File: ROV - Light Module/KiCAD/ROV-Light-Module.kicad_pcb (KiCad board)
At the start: 2 copper layers, 73.7 x 23.4 mm, 55 parts, among them J4 Bottom - Middle, J6 Main In, J7 Bottom - Middle, J8 Middle - Top, J9 Middle - Top, U1 AL8805W5, U2 ATtiny1614-Arduino, U3 AP63205WU, U6 MAX3072E

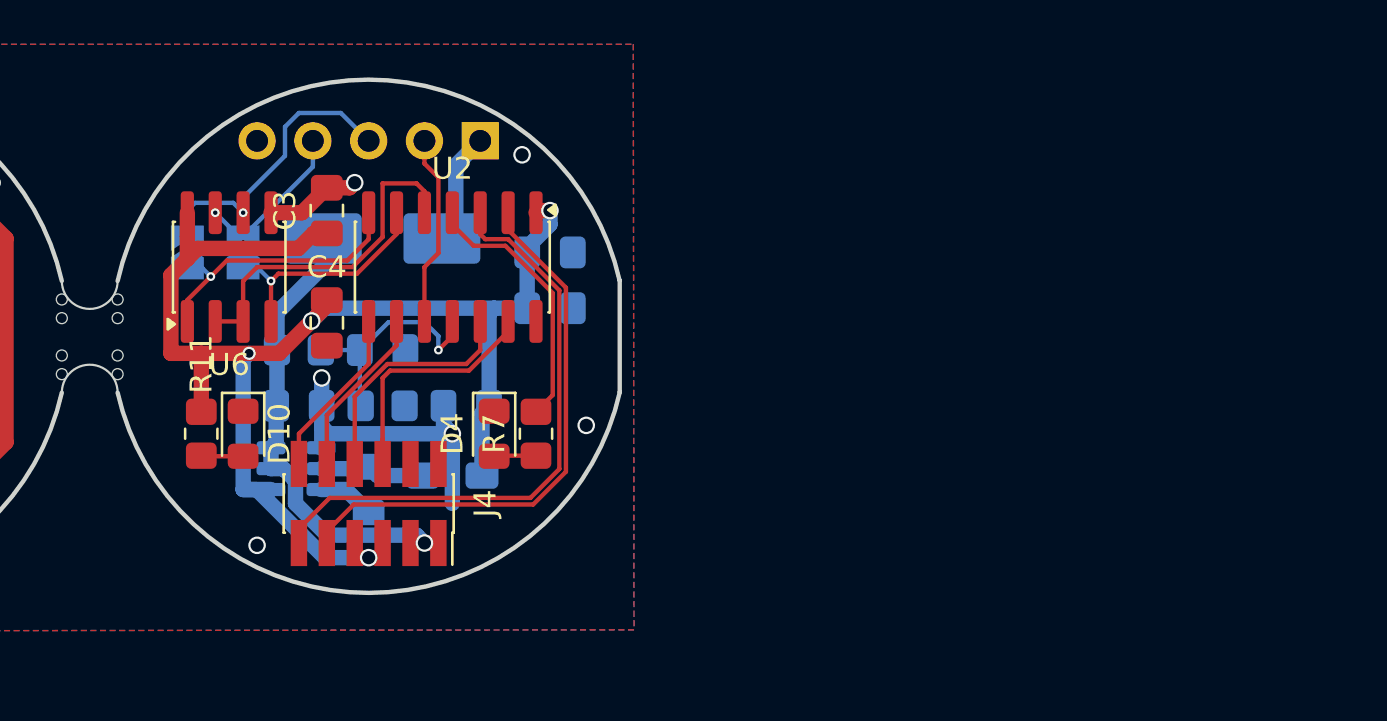
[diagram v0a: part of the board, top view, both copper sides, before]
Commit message: moved the arduino to seperet schematic
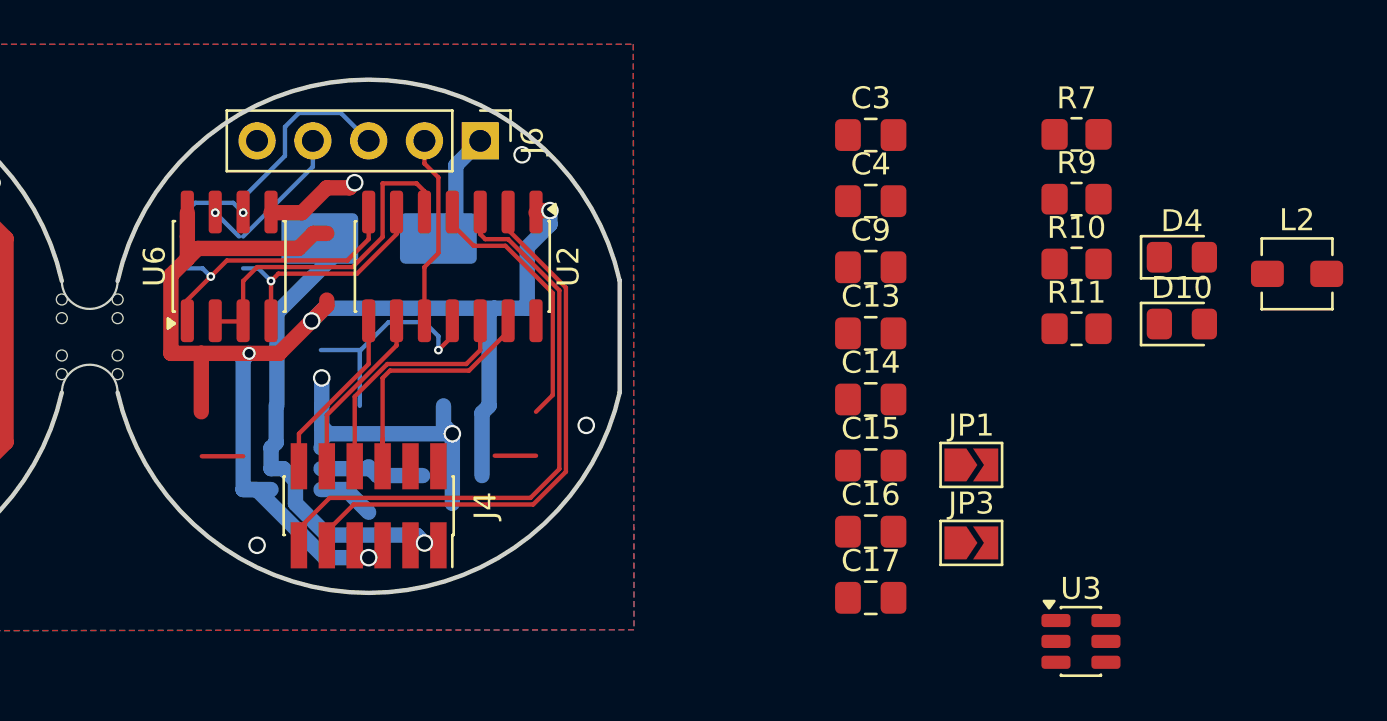
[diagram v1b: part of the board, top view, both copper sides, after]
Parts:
- removed JP2: RX, Jumper:SolderJumper-2_P1.3mm_Open_TrianglePad1.0x1.5mm
- added JP3: RX, Jumper:SolderJumper-2_P1.3mm_Open_TrianglePad1.0x1.5mm, F.Cu at (217.9, 85.6)
- C13, C14, C15, C16, C17, C9, J6, JP1, L2, R10, R9, U3: moved to F.Cu
- moved D10 43.0 mm to (227.5, 75.7), turned to 0 degrees
- moved R11 40.1 mm to (222.7, 75.9), turned to 0 degrees
- moved L2 39.5 mm to (232.8, 73.4)
- moved JP1 37.0 mm to (217.9, 82.1), turned to 0 degrees
- moved U3 36.6 mm to (222.9, 90.1)
- moved R9 36.1 mm to (222.7, 70.0)
- moved D4 32.3 mm to (227.5, 72.6), turned to 0 degrees
- moved R10 32.2 mm to (222.7, 72.9)
- moved R7 28.1 mm to (222.7, 67.0), turned to 0 degrees
- moved C14 26.0 mm to (213.4, 79.1), turned to 0 degrees
- moved C4 25.4 mm to (213.4, 70.1), turned to 0 degrees
- moved C3 25.0 mm to (213.4, 67.0), turned to 0 degrees
- moved C15 22.9 mm to (213.4, 82.1), turned to 0 degrees
- moved C13 22.2 mm to (213.4, 76.1)
- moved C17 21.5 mm to (213.4, 88.1), turned to 0 degrees
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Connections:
- net /A9/D9 renamed /Arduino Driver PCB/A9/D9
- net /Builtin_LED renamed /Arduino Driver PCB/Builtin_LED
- net /Data_A renamed /Arduino Driver PCB/Data_A
- net /Data_B renamed /Arduino Driver PCB/Data_B
- net /LED_PWM renamed /Arduino Driver PCB/LED_PWM
- net /NeoPixle renamed /Arduino Driver PCB/NeoPixle
- net /SCL renamed /Arduino Driver PCB/SCL
- net /SDA renamed /Arduino Driver PCB/SDA
- net /SERIAL_DIR renamed /Arduino Driver PCB/SERIAL_DIR
- net /SERIAL_RX renamed /Arduino Driver PCB/SERIAL_RX
- net /SERIAL_TX renamed /Arduino Driver PCB/SERIAL_TX
- net /STATUS_LED renamed /Arduino Driver PCB/STATUS_LED
- net /UPDI renamed /Arduino Driver PCB/UPDI
- net /Vmeasure renamed /Arduino Driver PCB/Vmeasure
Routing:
- net Net-(D5-A): track 4.90 -> 18.8 mm, vias 0 -> 2
- net GND: track 34.0 -> 20.1 mm, vias 21 -> 19

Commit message: design review
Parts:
- removed D2: BAT54S, Package_TO_SOT_SMD:SOT-23
- removed R5, R6: 0.5, Resistor_SMD:R_1206_3216Metric_Pad1.30x1.75mm_HandSolder
- added D3: ZLLS1000TA, Package_TO_SOT_SMD:SOT-23, F.Cu at (170.8, 74.9)
- added J1: AVR UPDI Header, Connector_PinHeader_2.54mm:PinHeader_2x03_P2.54mm_Vertical, F.Cu at (190.5, 96.5)
- moved L2 26.5 mm to (207.6, 81.9)
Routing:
- net /LED-_L: track 12.0 -> 13.8 mm
- net V_in_Mid: track 33.2 -> 31.9 mm
- net /LED_SW: track 10.9 -> 12.2 mm

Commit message: updates
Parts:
- removed JP1: TX, Jumper:SolderJumper-2_P1.3mm_Open_TrianglePad1.0x1.5mm
- removed JP3: RX, Jumper:SolderJumper-2_P1.3mm_Open_TrianglePad1.0x1.5mm
- C14, C15, C16, C17, C9, D10, D4, L2, R10, R11, R7, R9, U3: moved to B.Cu
- C3: value 100nF -> 10pF
- J1: footprint Connector_PinHeader_2.54mm:PinHeader_2x03_P2.54mm_Vertical -> Connector_PinHeader_1.27mm:PinHeader_2x03_P1.27mm_Vertical_SMD; moved to B.Cu
- J4: value Bottom - Middle -> Conn_02x05_Odd_Even; footprint Connector_PinSocket_1.27mm:PinSocket_2x06_P1.27mm_Vertical_SMD -> Connector_PinSocket_1.27mm:PinSocket_2x05_P1.27mm_Vertical_SMD
- moved D4 45.1 mm to (183.5, 82.5), turned to 90 degrees
- moved R10 42.1 mm to (181.0, 78.1), turned to -90 degrees
- moved R9 42.0 mm to (181.0, 74.3), turned to -90 degrees
- moved R7 40.4 mm to (185.4, 82.5), turned to -90 degrees
- moved U3 37.6 mm to (188.0, 76.2)
- moved C13 32.6 mm to (181.0, 79.4), turned to -90 degrees
- moved C4 31.3 mm to (183.5, 79.4), turned to -90 degrees
- moved C17 30.9 mm to (184.2, 78.1), turned to -90 degrees
- moved D10 30.8 mm to (197.5, 82.5), turned to 90 degrees
- moved C14 29.6 mm to (184.2, 74.3), turned to 90 degrees
- moved R11 28.0 mm to (195.6, 82.5), turned to -90 degrees
- moved C15 19.3 mm to (194.9, 76.2), turned to -90 degrees
- moved C16 19.2 mm to (197.5, 74.3), turned to 90 degrees
- moved L2 16.9 mm to (191.8, 76.2), turned to -90 degrees
- moved C3 15.2 mm to (200.0, 74.3), turned to -90 degrees
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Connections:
- net Net-(D5-A) renamed V_Supply
- J4 pad 10: /Arduino Driver PCB/SCL -> /Arduino Driver PCB/SDA
- J4 pad 3: V_in -> +5V
- J4 pad 5: +5V -> /Arduino Driver PCB/NeoPixle
- J4 pad 6: /Arduino Driver PCB/NeoPixle -> /Arduino Driver PCB/LED_PWM
- J4 pad 7: +5V -> /Arduino Driver PCB/A9/D9
- J4 pad 8: /Arduino Driver PCB/A9/D9 -> /Arduino Driver PCB/SCL
- J4 pad 9: /Arduino Driver PCB/LED_PWM -> /Arduino Driver PCB/STATUS_LED
- J6 pad 3: /Arduino Driver PCB/Data_A -> /Arduino Driver PCB/Data_B
- J6 pad 4: /Arduino Driver PCB/Data_B -> /Arduino Driver PCB/Data_A
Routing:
- net GND: track 20.1 -> 60.8 mm
- net V_Supply: track 18.8 -> 0.00 mm, vias 2 -> 0
- net /Arduino Driver PCB/SERIAL_TX: track 12.8 -> 26.3 mm
- net /Arduino Driver PCB/SERIAL_RX: track 10.9 -> 21.3 mm
- net /Arduino Driver PCB/Vmeasure: track 10.2 -> 20.4 mm, vias 1 -> 3
- net /Arduino Driver PCB/UPDI: track 8.75 -> 17.7 mm, vias 0 -> 1
- net V_in: track 20.7 -> 29.3 mm
- net /Arduino Driver PCB/LED_PWM: track 24.1 -> 15.6 mm
- net /Arduino Driver PCB/Data_B: track 7.20 -> 12.8 mm, vias 1 -> 0
- net /Arduino Driver PCB/Builtin_LED: track 11.6 -> 16.2 mm, vias 0 -> 1
- net Net-(U3-BST): track 2.60 -> 6.22 mm
- net /Arduino Driver PCB/A9/D9: track 11.0 -> 14.5 mm
- net /Arduino Driver PCB/Data_A: track 13.3 -> 10.8 mm, vias 1 -> 0
- net /Arduino Driver PCB/NeoPixle: track 12.3 -> 14.3 mm
- net /Arduino Driver PCB/STATUS_LED: track 26.8 -> 24.8 mm, vias 0 -> 2
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- added copper zone on B.Cu, net V_Supply
- added copper zone on B.Cu, net V_in

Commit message: cleanup
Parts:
- added R4: 0.5, Resistor_SMD:R_0805_2012Metric_Pad1.20x1.40mm_HandSolder, F.Cu at (165.1, 78.8)
- C13: moved to B.Cu
- J6: footprint Connector_PinHeader_2.54mm:PinHeader_1x05_P2.54mm_Vertical -> Connector_PinHeader_2.54mm:PinHeader_1x05_P2.54mm_Vertical_SMD_Pin1Left; moved to B.Cu
- R1, R2: footprint Resistor_SMD:R_1206_3216Metric_Pad1.30x1.75mm_HandSolder -> Resistor_SMD:R_0805_2012Metric_Pad1.20x1.40mm_HandSolder
- R9: value 37k -> 51k
- U6: value MAX3072E -> ADM485
- moved C3 19.1 mm to (181.0, 74.3)
- moved C9 17.5 mm to (183.5, 80.0), turned to 180 degrees
- moved C4 17.3 mm to (200.0, 74.3)
- moved C13 15.6 mm to (194.9, 72.4), turned to 0 degrees
- moved C16 14.3 mm to (183.5, 77.5), turned to 0 degrees
- moved D10 13.4 mm to (184.2, 83.2)
- moved D4 13.4 mm to (196.8, 83.2)
- moved R9 10.3 mm to (191.1, 72.4), turned to 180 degrees
- moved D5 10.2 mm to (199.4, 76.2), turned to 90 degrees
- moved R11 9.55 mm to (186.1, 83.2)
- moved R7 9.55 mm to (194.9, 83.2)
- moved R10 8.54 mm to (187.3, 72.4), turned to 180 degrees
- moved J6 5.12 mm to (190.5, 67.9), turned to 90 degrees
- moved C17 3.24 mm to (183.5, 74.9), turned to 0 degrees
- moved C14 2.01 mm to (183.5, 72.4), turned to 0 degrees
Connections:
- U6 pad 1: /Arduino Driver PCB/SERIAL_TX -> /Arduino Driver PCB/SERIAL_RX
- U6 pad 4: /Arduino Driver PCB/SERIAL_RX -> /Arduino Driver PCB/SERIAL_TX
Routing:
- net GND: track 60.8 -> 36.8 mm, vias 19 -> 21
- net +5V: track 63.3 -> 79.9 mm, vias 4 -> 2
- net /Arduino Driver PCB/Vmeasure: track 20.4 -> 9.60 mm, vias 3 -> 1
- net /Arduino Driver PCB/SERIAL_RX: track 21.3 -> 30.0 mm
- net /Arduino Driver PCB/UPDI: track 17.7 -> 23.1 mm, vias 1 -> 2
- net /Arduino Driver PCB/Data_A: track 10.8 -> 6.22 mm, vias 0 -> 1
- net V_in: track 29.3 -> 33.7 mm
- net /Arduino Driver PCB/SERIAL_TX: track 26.3 -> 30.6 mm
- net /Arduino Driver PCB/Data_B: track 12.8 -> 9.66 mm, vias 0 -> 1
- net /Arduino Driver PCB/Builtin_LED: track 16.2 -> 14.0 mm
- net /Arduino Driver PCB/STATUS_LED: track 24.8 -> 26.8 mm, vias 2 -> 1
- net /Arduino Driver PCB/LED_PWM: track 15.6 -> 16.2 mm
- removed copper zone on B.Cu, net V_in

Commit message: update PCBs
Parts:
- U6: value ADM485 -> MAX13487E
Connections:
- net /Arduino Driver PCB/A9/D9 renamed /A9/D9
- net /Arduino Driver PCB/LED_PWM renamed /LED_PWM
- net /Arduino Driver PCB/NeoPixle renamed /NeoPixle
- net /Arduino Driver PCB/SCL renamed /SCL
- net /Arduino Driver PCB/SDA renamed /SDA
- J1 pad 3: /Arduino Driver PCB/STATUS_LED -> /Arduino Driver PCB/Builtin_LED
- J4 pad 9: /Arduino Driver PCB/STATUS_LED -> /STATUS_LED
- U2 pad 3: /Arduino Driver PCB/STATUS_LED -> /STATUS_LED
- U2 pad 5: /Arduino Driver PCB/SERIAL_DIR -> /Arduino Driver PCB/A3/D3
- U6 pad 2: /Arduino Driver PCB/SERIAL_DIR -> +5V
- U6 pad 3: /Arduino Driver PCB/SERIAL_DIR -> +5V
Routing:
- net +5V: track 79.9 -> 34.8 mm, vias 2 -> 1
- net /Arduino Driver PCB/STATUS_LED: track 26.8 -> 0.00 mm, vias 1 -> 0
- net /STATUS_LED: track 0.00 -> 22.4 mm
- net GND: track 36.8 -> 54.1 mm, vias 21 -> 20
- net /Arduino Driver PCB/SERIAL_DIR: track 14.9 -> 0.00 mm
- net /Arduino Driver PCB/SERIAL_TX: track 30.6 -> 20.8 mm
- net /Arduino Driver PCB/Builtin_LED: track 14.0 -> 18.6 mm
- net /LED+_L: track 29.7 -> 25.8 mm
- net /A9/D9: track 14.5 -> 17.7 mm
- net Net-(U1-CTRL): track 8.80 -> 10.9 mm
- net V_in_Mid: track 31.9 -> 33.9 mm
- net V_in: track 33.7 -> 35.3 mm
- net /Arduino Driver PCB/SERIAL_RX: track 30.0 -> 28.7 mm
- net +5V_Mid: track 29.2 -> 30.3 mm
- net /Arduino Driver PCB/UPDI: track 23.1 -> 24.1 mm
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- added copper zone on F.Cu, net +5V
- added copper zone on B.Cu, net V_in

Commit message: Update ROV-Light-Module.kicad_pcb
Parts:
- J7: value Bottom - Middle -> Conn_02x05_Odd_Even; footprint Connector_PinHeader_1.27mm:PinHeader_2x06_P1.27mm_Vertical_SMD -> Connector_PinHeader_1.27mm:PinHeader_2x05_P1.27mm_Vertical_SMD
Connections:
- J7 pad 3: V_in_Mid -> +5V_Mid
- J7 pad 5: +5V_Mid -> /Neo_Mid
- J7 pad 6: /Neo_Mid -> /PWM
- J7 pad 7: +5V_Mid -> unconnected-(J7-Pin_7-Pad7)
- J7 pad 9: /PWM -> /STATUS
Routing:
- net /PWM: track 22.1 -> 18.2 mm
- net +5V_Mid: track 30.3 -> 27.3 mm
- net /STATUS: track 28.0 -> 28.8 mm
- net V_in_Mid: track 33.9 -> 33.3 mm
- net GND: vias 20 -> 19

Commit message: massive cleanup
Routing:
- net +5V: track 34.8 -> 36.4 mm
- net GND: track 54.1 -> 53.2 mm
- net /Arduino Driver PCB/Builtin_LED: track 18.6 -> 17.8 mm

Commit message: .
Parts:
- added R15: 4k7, Resistor_SMD:R_0805_2012Metric_Pad1.20x1.40mm_HandSolder, F.Cu at (188.0, 66.0)
- added R16: 470, Resistor_SMD:R_0805_2012Metric_Pad1.20x1.40mm_HandSolder, F.Cu at (193.0, 66.0)
- added R17: 470, Resistor_SMD:R_0805_2012Metric_Pad1.20x1.40mm_HandSolder, F.Cu at (193.0, 67.9)
- added R18: 470, Resistor_SMD:R_0805_2012Metric_Pad1.20x1.40mm_HandSolder, F.Cu at (188.0, 67.9)
- turned C3 to 90 degrees
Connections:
- U2 pad 5: /Arduino Driver PCB/A3/D3 -> /Function
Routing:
- net +5V: track 36.4 -> 49.6 mm, vias 1 -> 4
- net /Function: track 0.00 -> 12.0 mm, vias 0 -> 2
- net GND: track 53.2 -> 64.0 mm, vias 19 -> 20
- net /Arduino Driver PCB/Builtin_LED: track 17.8 -> 22.0 mm
- net /SDA: track 7.65 -> 9.37 mm
- net /Arduino Driver PCB/Data_B: track 9.66 -> 7.96 mm
- net /Arduino Driver PCB/Data_A: track 6.22 -> 7.35 mm
- net /Arduino Driver PCB/A3/D3: track 0.97 -> 0.00 mm
- net /STATUS_LED: track 22.4 -> 21.5 mm
